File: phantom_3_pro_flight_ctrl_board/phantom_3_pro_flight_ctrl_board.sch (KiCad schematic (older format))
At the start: 6 parts, among them J8 CONN_MC_FRONT, J9 CONN_MC_BACK

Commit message: Flight Ctrl: drawn DC conv and better uC schematic.
DC-DC converters have now some of surroundings mapped.
Also, the main uC schematic was divided into 4 parts
and properly defined.
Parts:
- removed S?: STM32F427IIH6, symbol STM32F4XXI2_A
- added R? (x3): 10kΩ, symbol R_Small
- added R?: 15,7kΩ, symbol R_Small
- added R?: 100Ω, symbol R_Small
- added R? (x2): 22Ω, symbol R_Small
- added TP?: PB10, symbol TEST
- added TP?: SWCLK, symbol TEST
- added TP? (x4): GND, symbol TEST
- added TP?: DAC_OUT, symbol TEST
- added TP?: 3V3A, symbol TEST
- added TP?: U3_RX, symbol TEST
- added TP?: U3_TX, symbol TEST
- added TP?: BOOT0, symbol TEST
- added TP?: 5V, symbol TEST
- added TP?: VCC3V6, symbol TEST
- added TP?: U7_RX, symbol TEST
- added TP?: U7_TX, symbol TEST
- added TP?: CAN1_T, symbol TEST
- added TP?: SWDIO, symbol TEST
- added TP?: CAN1_R, symbol TEST
- added TP?: PB11, symbol TEST
- added TP?: VCC3V3, symbol TEST
- added U?: STM32F427II_0, symbol STM32F4XXH2
- added U?: STM32F427II_A, symbol STM32F4XXH2_A
- added U?: STM32F427II_B, symbol STM32F4XXH2_B
- added U?: STM32F427II_C, symbol STM32F4XXH2_C
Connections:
- net labels added: 1V2, 3V3A, VCC3V3
- net labels removed: 3V6?
- wire segments 47 -> 125
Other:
- moved on the sheet: J9, J?, U?

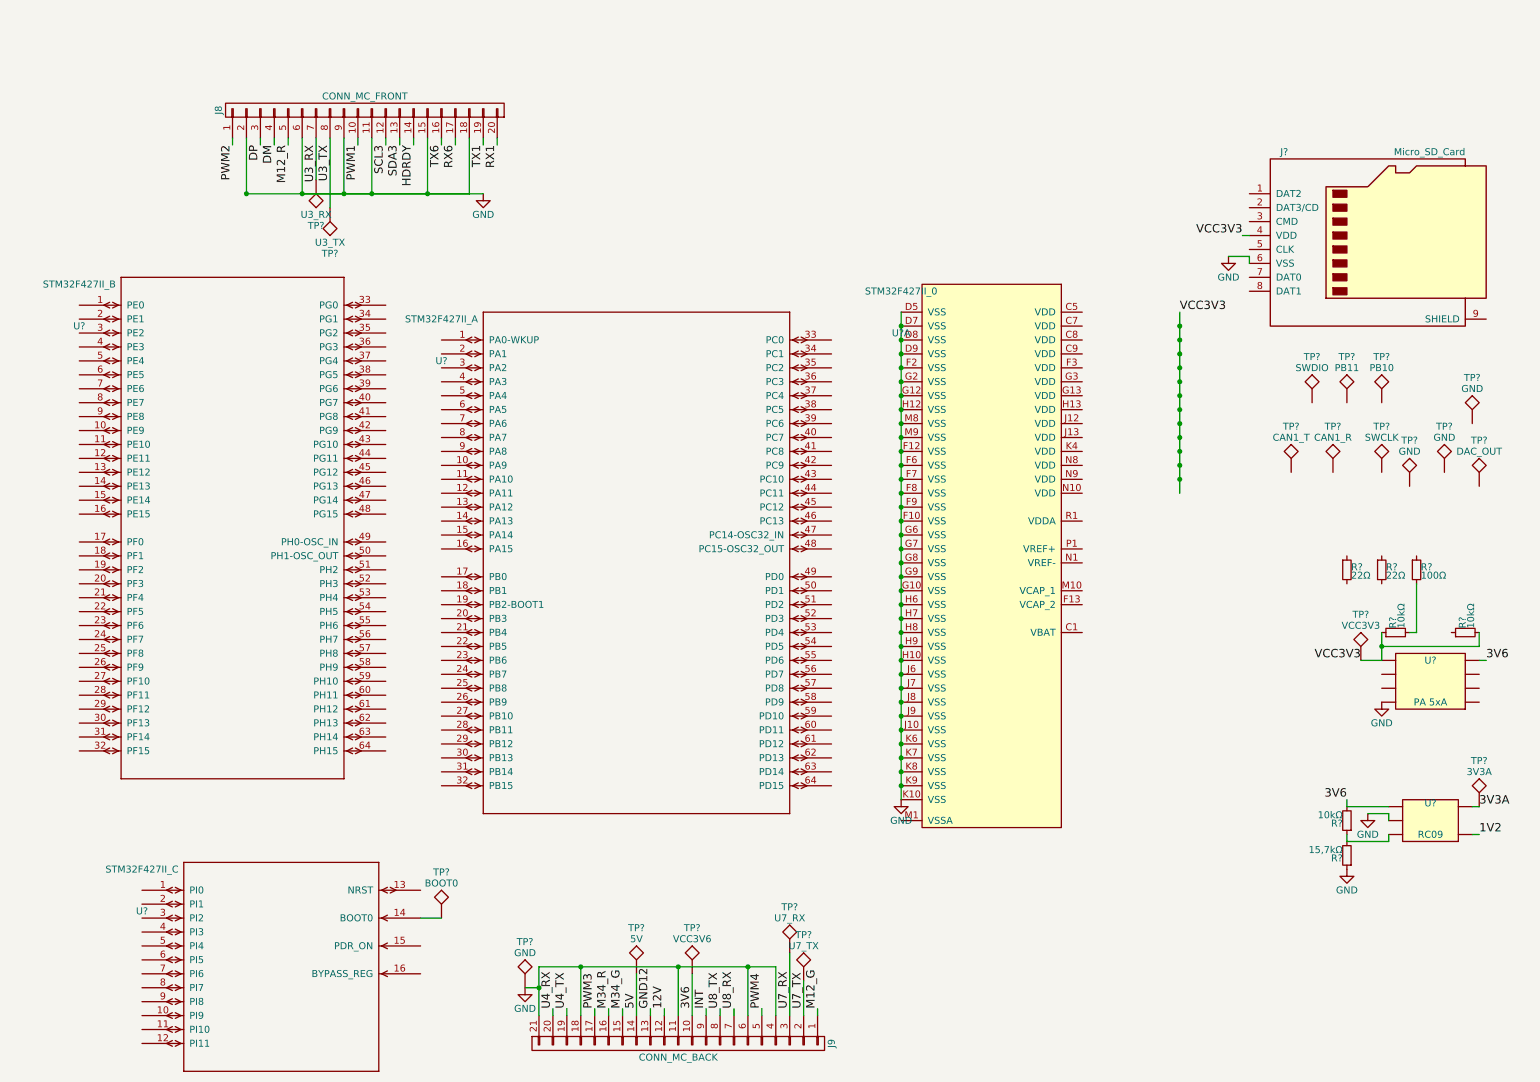
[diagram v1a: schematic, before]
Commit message: Flight Ctrl: Started work on PCB.
WIP on edge connectors.
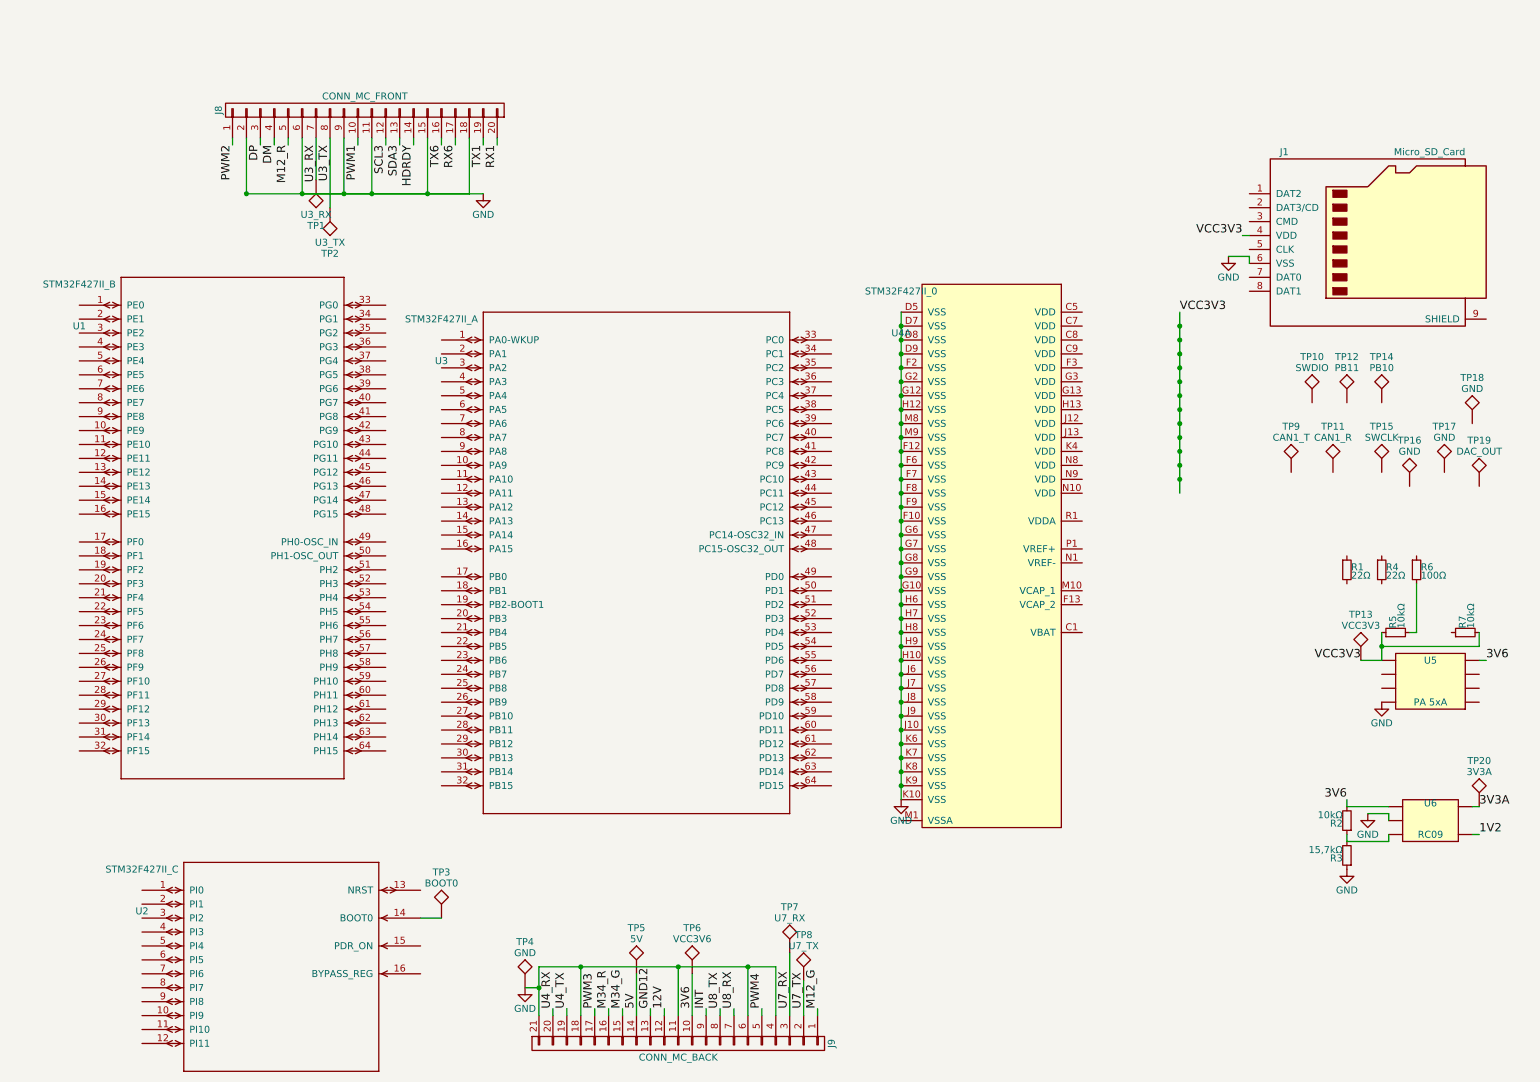
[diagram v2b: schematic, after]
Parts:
- removed TP?: PB10, symbol TEST
- removed TP?: SWCLK, symbol TEST
- removed TP? (x4): GND, symbol TEST
- removed TP?: DAC_OUT, symbol TEST
- removed TP?: 3V3A, symbol TEST
- removed TP?: U3_RX, symbol TEST
- removed TP?: U3_TX, symbol TEST
- removed TP?: BOOT0, symbol TEST
- removed TP?: 5V, symbol TEST
- removed TP?: VCC3V6, symbol TEST
- removed TP?: U7_RX, symbol TEST
- removed TP?: U7_TX, symbol TEST
- removed TP?: CAN1_T, symbol TEST
- removed TP?: SWDIO, symbol TEST
- removed TP?: CAN1_R, symbol TEST
- removed TP?: PB11, symbol TEST
- removed TP?: VCC3V3, symbol TEST
- added TP1: U3_RX, Connectors:1pin, symbol TEST
- added TP10: SWDIO, Connectors:1pin, symbol TEST
- added TP11: CAN1_R, Connectors:1pin, symbol TEST
- added TP12: PB11, Connectors:1pin, symbol TEST
- added TP13: VCC3V3, Connectors:1pin, symbol TEST
- added TP14: PB10, Connectors:1pin, symbol TEST
- added TP15: SWCLK, Connectors:1pin, symbol TEST
- added TP16, TP17, TP18, TP4: GND, Connectors:1pin, symbol TEST
- added TP19: DAC_OUT, Connectors:1pin, symbol TEST
- added TP2: U3_TX, Connectors:1pin, symbol TEST
- added TP20: 3V3A, Connectors:1pin, symbol TEST
- added TP3: BOOT0, Connectors:1pin, symbol TEST
- added TP5: 5V, Connectors:1pin, symbol TEST
- added TP6: VCC3V6, Connectors:1pin, symbol TEST
- added TP7: U7_RX, Connectors:1pin, symbol TEST
- added TP8: U7_TX, Connectors:1pin, symbol TEST
- added TP9: CAN1_T, Connectors:1pin, symbol TEST
- R1, R2, R3, R4, R5, R6, R7: renamed from R?; footprint (none) -> Resistors_SMD:R_0201
- U4: renamed from U?; footprint (none) -> Housings_BGA_custom:BGA-176p25_10x10_11.0x11.0mm_Pitch0.65mm
- U5, U6: renamed from U?; footprint MODULE -> (none)
- gave numbers to parts that had none: 4
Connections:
- net 3V3A: now also TP20.1
- net 3V6: now also TP6.1
- net 5V: now also TP5.1
- net GND: now also TP4.1
- net U3_RX: now also TP1.1
- net U3_TX: now also TP2.1
- net U7_RX: now also TP7.1
- net U7_TX: now also TP8.1
- net VCC3V3: now also TP13.1
- net at U2.14 (BOOT0): now also TP3.1
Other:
- moved on the sheet: TP1

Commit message: Flight Ctrl: Updated uC component to map to BGA.
The microcontroller model was updated so that pin numbers map
to numbers in BGA footprint.

Also, edge pad connector footprints were updated.
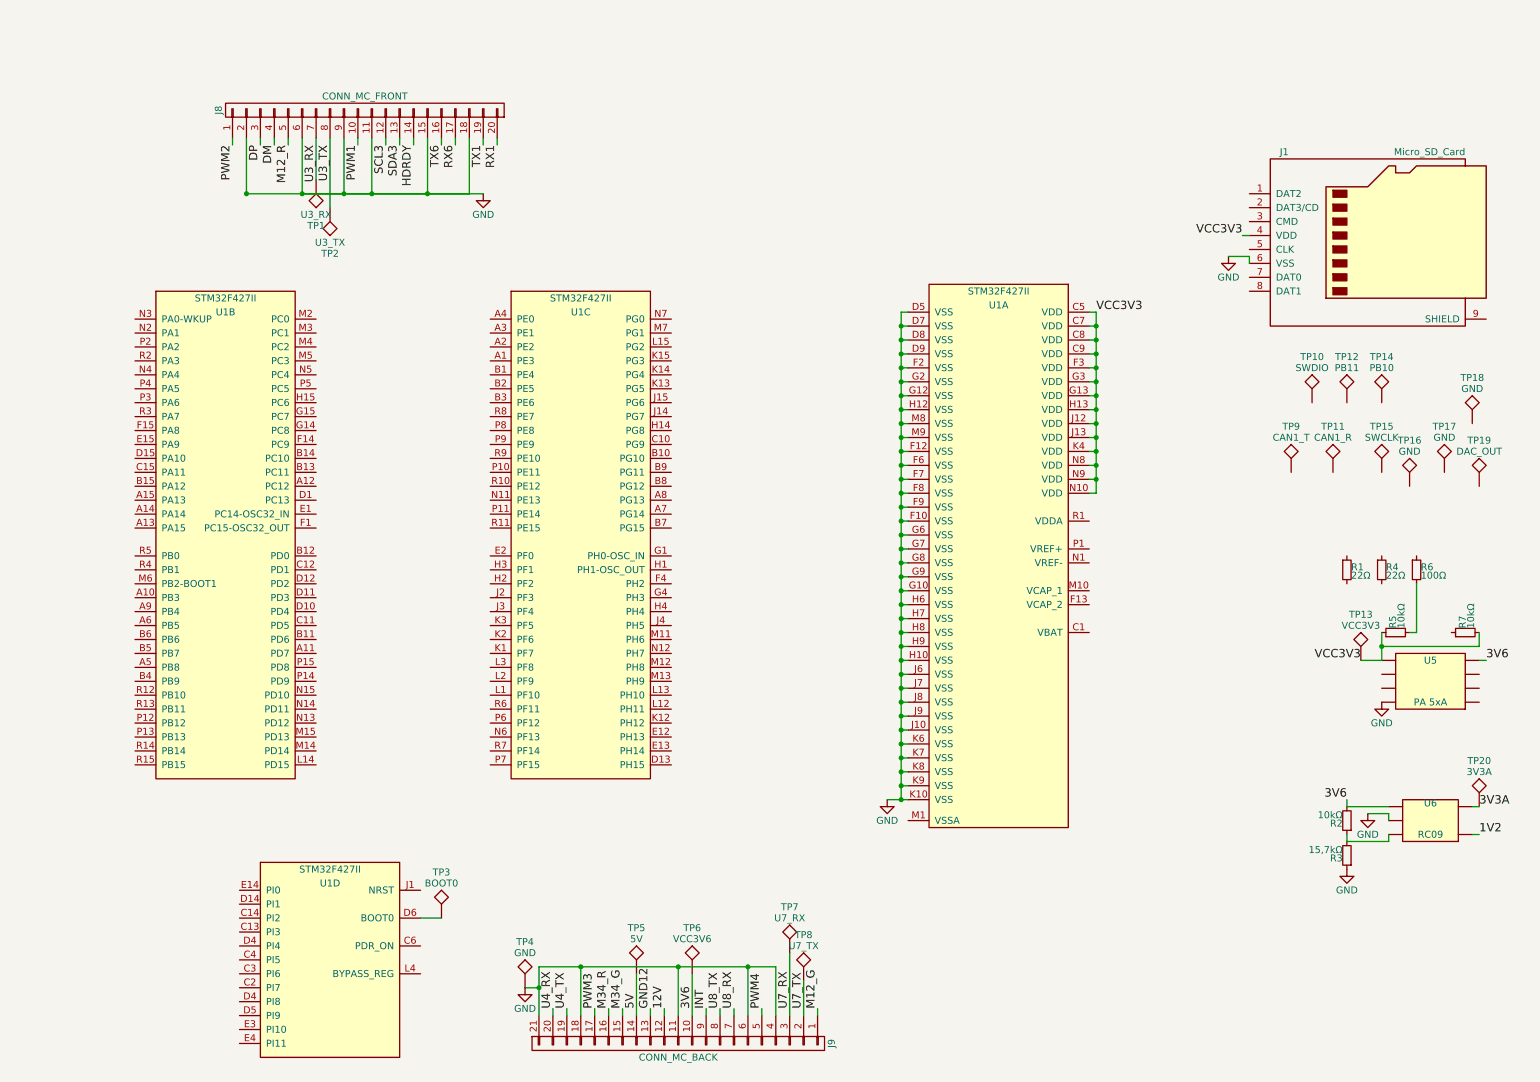
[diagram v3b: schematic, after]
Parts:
- removed U1: STM32F427II_B, symbol STM32F4XXH2_B
- removed U2: STM32F427II_C, symbol STM32F4XXH2_C
- removed U3: STM32F427II_A, symbol STM32F4XXH2_A
- removed U4: STM32F427II_0, Housings_BGA_custom:BGA-176p25_10x10_11.0x11.0mm_Pitch0.65mm, symbol STM32F4XXH2
- added U1: STM32F427II, Housings_BGA_custom:BGA-176p25_10x10_11.0x11.0mm_Pitch0.65mm, symbol STM32F4XXH2
- J8: footprint (none) -> Connectors_custom:Connector-edge-20pin-1.78mm-cut
- J9: footprint (none) -> Connectors_custom:Connector-edge-21pin-1.78mm-cut
- TP1, TP10, TP12, TP14, TP15, TP17, TP18, TP19, TP2, TP20, TP3, TP6, TP7, TP8: footprint Connectors:1pin -> Measurement_Points:Measurement_Point_Round-SMD-Pad_Small
- TP11, TP13, TP16, TP4, TP5, TP9: footprint Connectors:1pin -> Measurement_Points:Measurement_Point_Round-SMD-Pad_Big
- U5: footprint (none) -> Housings_DFN_QFN:DFN-8-1EP_3x3mm_Pitch0.65mm
- U6: footprint (none) -> TO_SOT_Packages_SMD:TSOT-23-5
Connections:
- net GND: now also U1.D5 (VSS), U1.D7 (VSS), U1.D8 (VSS), U1.D9 (VSS), U1.F10 (VSS), U1.F12 (VSS), U1.F2 (VSS), U1.F6 (VSS), U1.F7 (VSS), U1.F8 (VSS), U1.F9 (VSS), U1.G10 (VSS), U1.G12 (VSS), U1.G2 (VSS), U1.G6 (VSS), U1.G7 (VSS), U1.G8 (VSS), U1.G9 (VSS), U1.H10 (VSS), U1.H12 (VSS), U1.H6 (VSS), U1.H7 (VSS), U1.H8 (VSS), U1.H9 (VSS), U1.J10 (VSS), U1.J6 (VSS), U1.J7 (VSS), U1.J8 (VSS), U1.J9 (VSS), U1.K10 (VSS), U1.K6 (VSS), U1.K7 (VSS), U1.K8 (VSS), U1.K9 (VSS), U1.M8 (VSS), U1.M9 (VSS)
- net VCC3V3: now also U1.C5 (VDD), U1.C7 (VDD), U1.C8 (VDD), U1.C9 (VDD), U1.F3 (VDD), U1.G13 (VDD), U1.G3 (VDD), U1.H13 (VDD), U1.J12 (VDD), U1.J13 (VDD), U1.K4 (VDD), U1.N10 (VDD), U1.N8 (VDD), U1.N9 (VDD)
- net at TP3.1: now also U1.D6 (BOOT0)

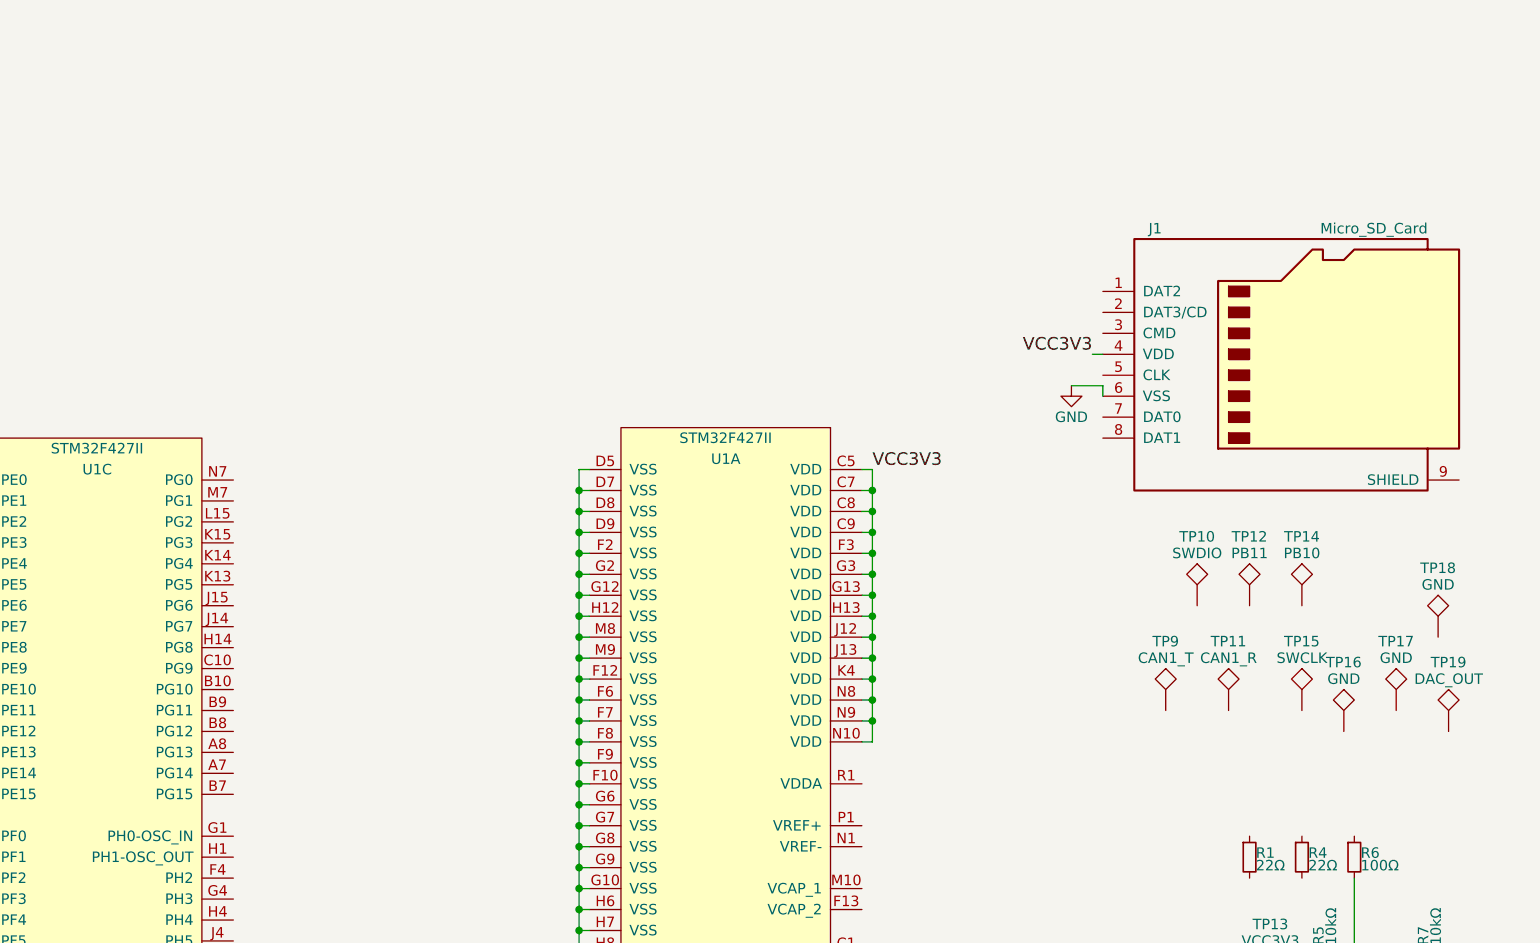
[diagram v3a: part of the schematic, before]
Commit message: Flight Ctrl: Added SD card and IMU.
The IMU is placed on separate board, but there are
footprints on the flight controller PCB to solder
it directly as well.
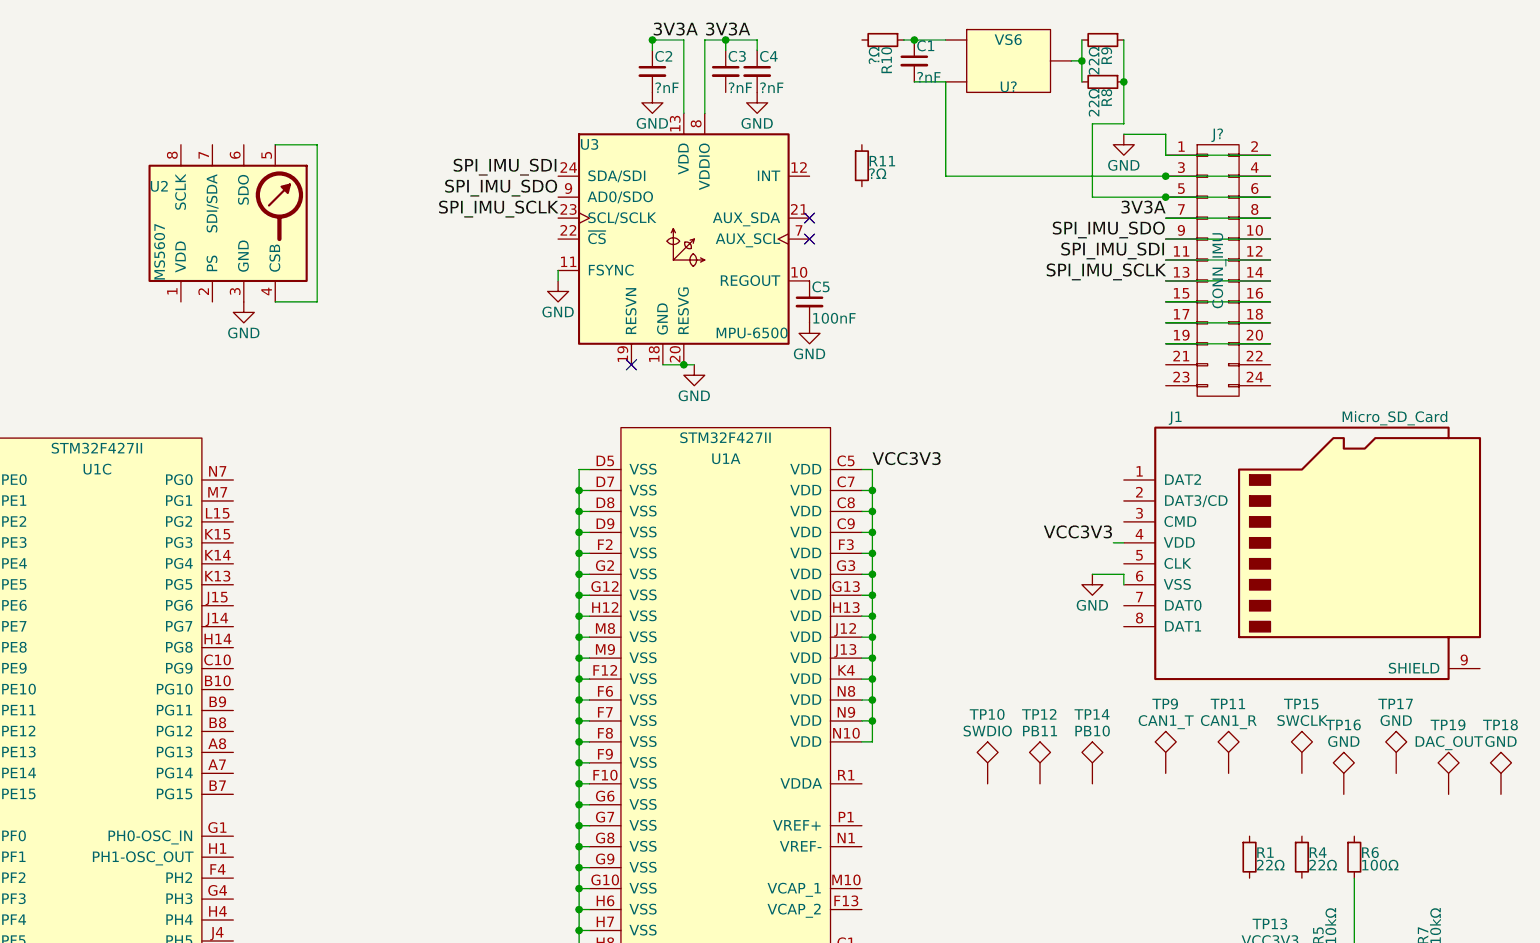
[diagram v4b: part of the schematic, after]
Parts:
- added C1, C2, C3, C4: ?nF, Capacitors_SMD:C_0201, symbol C_Small
- added C5: 100nF, Capacitors_SMD:C_0201, symbol C_Small
- added J?: CONN_IMU, symbol CONN_02X12
- added R10, R11: ?Ω, Resistors_SMD:R_0201, symbol R_Small
- added R8, R9: 22Ω, Resistors_SMD:R_1206, symbol R_Small
- added U2: MS5607, Housings_LGA:LGA-8_3x5mm_Pitch1.25mm, symbol MS5607_Anno
- added U3: MPU-6500, Housings_DFN_QFN:QFN-24_3x3mm_Pitch0.4mm, symbol MPU-6500
- added U?: VS6, MODULE, symbol IC_SOT3
- J1: footprint (none) -> Connectors:microSD_Card_Receptacle_Wuerth_693072010801
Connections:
- net 3V3A: now also C2.1, C3.1, C4.1, J?.7 (P7), J?.8 (P8), U3.13 (VDD), U3.8 (VDDIO)
- net GND: now also C2.2, C4.2, C5.2, J?.1 (P1), J?.2 (P2), U2.3 (GND), U3.11 (FSYNC), U3.14 (NC), U3.18 (GND), U3.20 (RESVG)
- new net: U2.4 (CSB), U2.5
- new net: C5.1, U3.10 (REGOUT)
- new net: J?.5 (P5), J?.6 (P6), R8.1, R9.1
- new net: R8.2, R9.2, U?.3
- new net: C1.1, R10.1, U?.1
- new net: C1.2, J?.3 (P3), J?.4 (P4), U?.2
- new net: J?.15 (P15), J?.16 (P16)
- new net: J?.17 (P17), J?.18 (P18)
- new net: J?.19 (P19), J?.20 (P20)
- new net SPI_IMU_SCLK: J?.13 (P13), J?.14 (P14), U3.23 (SCL/SCLK)
- new net SPI_IMU_SDI: J?.11 (P11), J?.12 (P12), U3.24 (SDA/SDI)
- new net SPI_IMU_SDO: J?.10 (P10), J?.9 (P9), U3.9 (AD0/SDO)
- no-connect marks 0 -> 3
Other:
- moved on the sheet: J1, TP10, TP11, TP12, TP14, TP15, TP16, TP17, TP18, TP19, TP9
